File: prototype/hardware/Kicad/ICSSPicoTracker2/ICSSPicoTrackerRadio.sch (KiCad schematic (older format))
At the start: 85 parts, among them U11 74LVC1G04, U4 PE4259, U5 PE4259, U6 SX1276

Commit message: Updated Scehematics and Footprints
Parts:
- removed V01, V02, V03, V04, V05, V06: V-RF, symbol ICSSPicoTracker:V-RF
- added ANT?: Johanson434, symbol ICSSPicoTracker:Johanson434
- added ANT?: Johanson868, symbol ICSSPicoTracker:Johanson868
- added C75: 100nF, Capacitor_SMD:C_0603_1608Metric, symbol Device:C
- added X2: IQXO-70, Oscillator:Oscillator_SMD_SeikoEpson_SG210-4Pin_2.5x2.0mm, symbol Oscillator:IQXO-70
- C10, C11, C12, C14, C61, C8: value 100n -> 100nF; footprint (none) -> Capacitor_SMD:C_0603_1608Metric
- C13, C19, C31, C32, C42, C43, C50, C51, C57, C58, C59: value 47p -> 47pF; footprint (none) -> Capacitor_SMD:C_0402_1005Metric
- C15: value 10nf -> 10nF; footprint (none) -> Capacitor_SMD:C_0402_1005Metric
- C16, C17, C24: value 8p2 -> 8.2pF; footprint (none) -> Capacitor_SMD:C_0402_1005Metric
- C18: value 27p -> 27pF; footprint (none) -> Capacitor_SMD:C_0402_1005Metric
- C20: value 22p -> 22pF; footprint (none) -> Capacitor_SMD:C_0402_1005Metric
- C21: value 100p -> 100pF; footprint (none) -> Capacitor_SMD:C_0402_1005Metric
- C22, C26, C36, C37, C38, C40, C44, C45, C52, C53, C54, C55: footprint (none) -> Capacitor_SMD:C_0402_1005Metric
- C23: value 15p -> 15pF; footprint (none) -> Capacitor_SMD:C_0402_1005Metric
- C25, C35: value 56p -> 56pF; footprint (none) -> Capacitor_SMD:C_0402_1005Metric
- C27, C34: value 3p3 -> 3.3pF; footprint (none) -> Capacitor_SMD:C_0402_1005Metric
- C28: value 2p7 -> 2.7pF; footprint (none) -> Capacitor_SMD:C_0402_1005Metric
- C29: value 1p5 -> 1.5pF; footprint (none) -> Capacitor_SMD:C_0402_1005Metric
- C30, C39, C60: value 4p7 -> 4.7pF; footprint (none) -> Capacitor_SMD:C_0402_1005Metric
- C33: value 12p -> 12pF; footprint (none) -> Capacitor_SMD:C_0402_1005Metric
- C41: value 33p -> 33pF; footprint (none) -> Capacitor_SMD:C_0402_1005Metric
- C46, C47, C48, C49: value 1n -> 1nF; footprint (none) -> Capacitor_SMD:C_0402_1005Metric
- C56: value 220p -> 220pF; footprint (none) -> Capacitor_SMD:C_0402_1005Metric
- L10: value 10n -> 10nH; footprint (none) -> Inductor_SMD:L_0402_1005Metric
- L11: value 12n -> 12nH; footprint (none) -> Inductor_SMD:L_0402_1005Metric
- L12: value 4n7 -> 4.7nH; footprint (none) -> Inductor_SMD:L_0402_1005Metric
- L13, L16, L2, L8: value 47n -> 47nH; footprint (none) -> Inductor_SMD:L_0402_1005Metric
- L14, L5: value 18n -> 18nH; footprint (none) -> Inductor_SMD:L_0402_1005Metric
- L15, L17, L18, L19, L9: footprint (none) -> Inductor_SMD:L_0402_1005Metric
- L3: value 33n -> 33nH; footprint (none) -> Inductor_SMD:L_0402_1005Metric
- L4: value 100n -> 100nH; footprint (none) -> Inductor_SMD:L_0402_1005Metric
- L6: value 22n -> 22nH; footprint (none) -> Inductor_SMD:L_0402_1005Metric
- L7: value 5n6 -> 5.6nH; footprint (none) -> Inductor_SMD:L_0402_1005Metric
- R2, R3, R4, R5: footprint (none) -> Resistor_SMD:R_0603_1608Metric
- U11: footprint (none) -> Package_TO_SOT_SMD:SOT-353_SC-70-5
- U6: footprint (none) -> Package_DFN_QFN:QFN-28-1EP_6x6mm_P0.65mm_EP4.25x4.25mm_ThermalVias
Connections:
- net labels added: +1V8, RF_DIO0, RF_DIO1, RF_DIO2, RF_DIO3, RF_DIO4, RF_DIO5, RF_MISO, RF_MOSI, RF_NSEL, RF_RESET, RF_SCLK
- net labels removed: RF-CLK, RF-DIO0, RF-DIO5, RF-MISO, RF-MOSI, RF-NSEL, RF-RESET, RF-SCLK, RFSW-RX, RFSW-TX
- wire segments 257 -> 274
- no-connect marks 5 -> 3
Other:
- moved on the sheet: C14

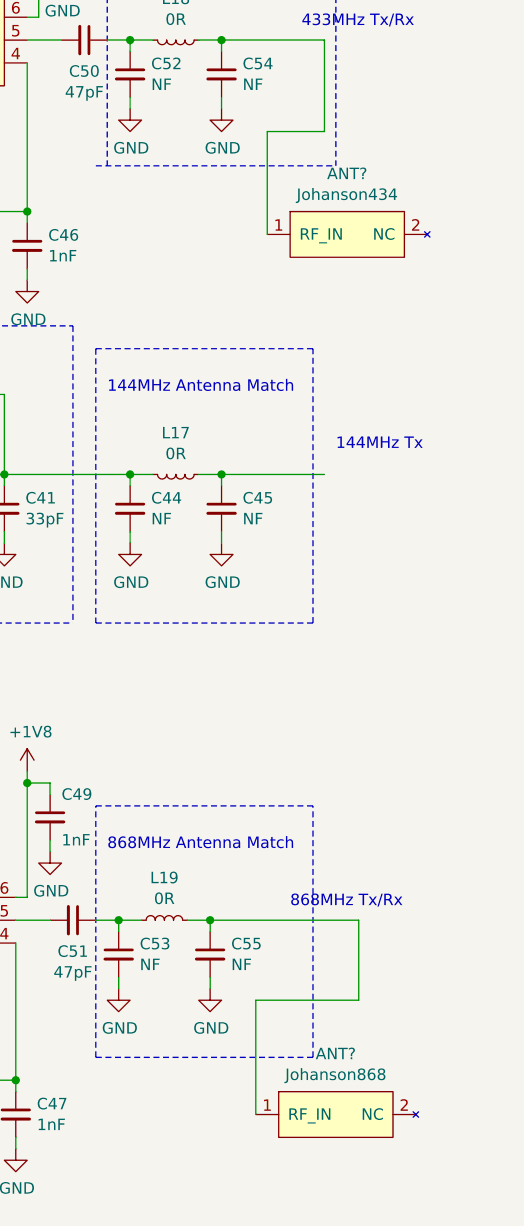
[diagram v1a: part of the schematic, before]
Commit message: Add Antenna footprints
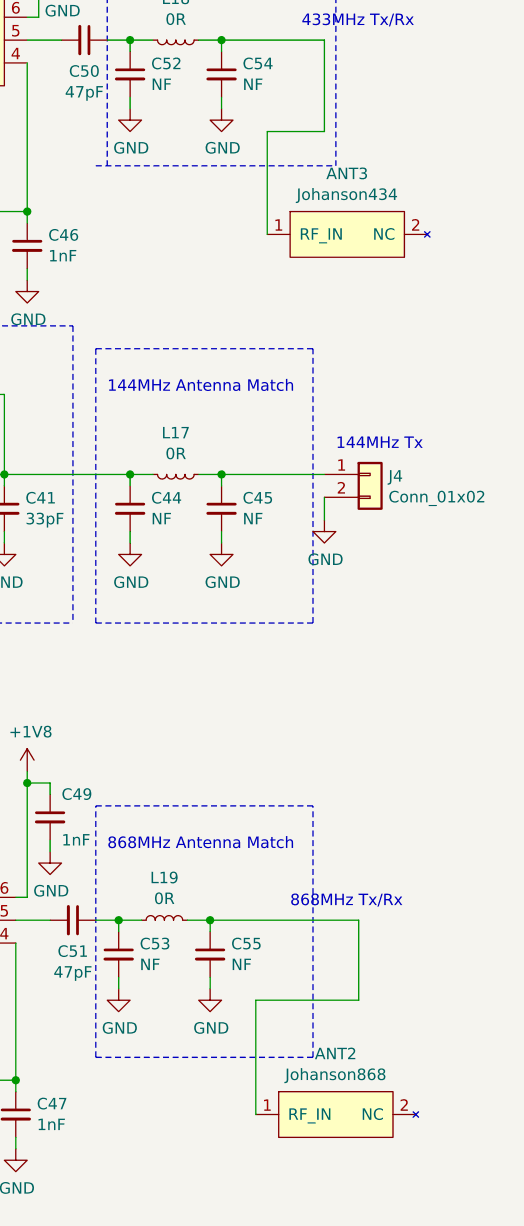
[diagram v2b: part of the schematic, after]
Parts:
- added J4: Conn_01x02, Connector_PinHeader_2.54mm:PinHeader_1x02_P2.54mm_Vertical, symbol Connector_Generic:Conn_01x02
- ANT2: renamed from ANT?; footprint (none) -> ICSSPicoTracker2:Johanson868
- ANT3: renamed from ANT?; footprint (none) -> ICSSPicoTracker2:Johanson434
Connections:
- net GND: now also J4.2 (Pin_2)
- net at C45.1, L17.1: now also J4.1 (Pin_1)
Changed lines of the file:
@@
 	1500 1750 1500 1800
 $Comp
-L ICSSPicoTracker:Johanson434 ANT?
+L ICSSPicoTracker:Johanson434 ANT3
 U 1 1 5D594580
 P 10850 2300
-F 0 "ANT?" H 10800 2565 50  0000 C CNN
+F 0 "ANT3" H 10800 2565 50  0000 C CNN
 F 1 "Johanson434" H 10800 2474 50  0000 C CNN
-F 2 "" H 10850 2300 50  0001 C CNN
+F 2 "ICSSPicoTracker2:Johanson434" H 10850 2300 50  0001 C CNN
 F 3 "" H 10850 2300 50  0001 C CNN
 	1    10850 2300
@@
 $EndComp
 $Comp
-L ICSSPicoTracker:Johanson868 ANT?
+L ICSSPicoTracker:Johanson868 ANT2
 U 1 1 5D59684D
 P 10800 6150
-F 0 "ANT?" H 10750 6415 50  0000 C CNN
+F 0 "ANT2" H 10750 6415 50  0000 C CNN
 F 1 "Johanson868" H 10750 6324 50  0000 C CNN
-F 2 "" H 10800 6150 50  0001 C CNN
+F 2 "ICSSPicoTracker2:Johanson868" H 10800 6150 50  0001 C CNN
 F 3 "" H 10800 6150 50  0001 C CNN
 	1    10800 6150
@@
 Wire Wire Line
 	10200 5300 10850 5300
+$Comp
+L Connector_Generic:Conn_01x02 J4
+U 1 1 5D5D0B50
+P 10900 3350
+F 0 "J4" H 10980 3342 50  0000 L CNN
+F 1 "Conn_01x02" H 10980 3251 50  0000 L CNN
+F 2 "Connector_PinHeader_2.54mm:PinHeader_1x02_P2.54mm_Vertical" H 10900 3350 50  0001 C CNN
+F 3 "~" H 10900 3350 50  0001 C CNN
+	1    10900 3350
+	1    0    0    -1
+$EndComp
+$Comp
+L power:GND #PWR0111
+U 1 1 5D5D1A65
+P 10700 3550
+F 0 "#PWR0111" H 10700 3300 50  0001 C CNN
+F 1 "GND" H 10705 3377 50  0000 C CNN
+F 2 "" H 10700 3550 50  0001 C CNN
+F 3 "" H 10700 3550 50  0001 C CNN
+	1    10700 3550
+	1    0    0    -1
+$EndComp
+Wire Wire Line
+	10700 3550 10700 3450
 $EndSCHEMATC

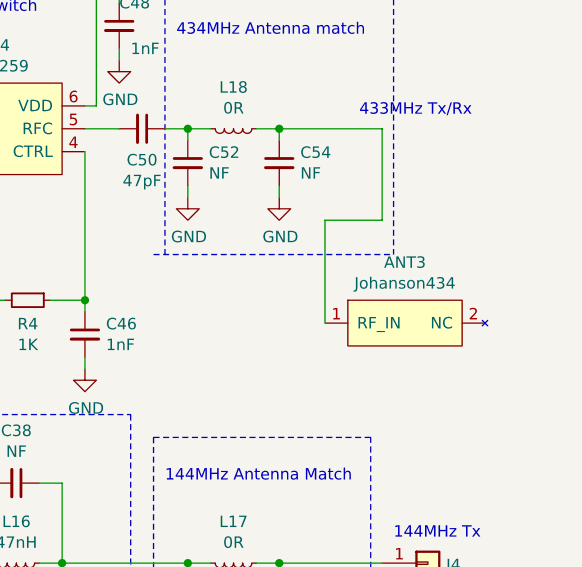
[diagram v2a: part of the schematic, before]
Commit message: Smaller Antenna and try some layouts
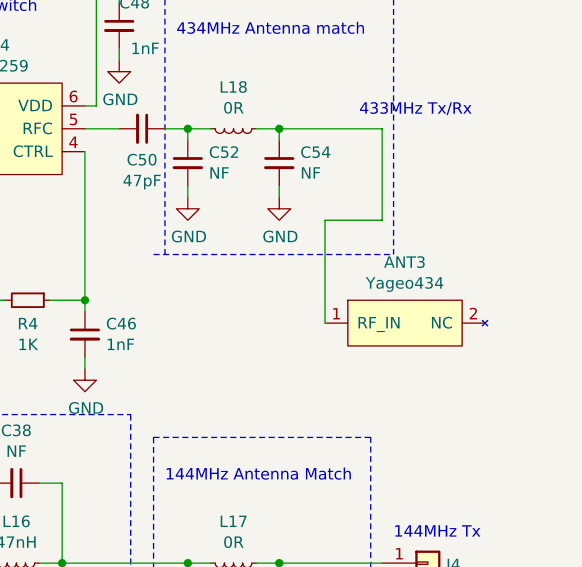
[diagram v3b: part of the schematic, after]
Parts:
- removed ANT3: Johanson434, ICSSPicoTracker2:Johanson434, symbol ICSSPicoTracker:Johanson434
- added ANT3: Yageo434, ICSSPicoTracker2:Yageo434, symbol ICSSPicoTracker:Yageo434
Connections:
- net at C54.1, L18.2: now also ANT3.1 (RF_IN)
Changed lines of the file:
@@
 	1500 1750 1500 1800
-$Comp
-L ICSSPicoTracker:Johanson434 ANT3
-U 1 1 5D594580
-P 10850 2300
-F 0 "ANT3" H 10800 2565 50  0000 C CNN
-F 1 "Johanson434" H 10800 2474 50  0000 C CNN
-F 2 "ICSSPicoTracker2:Johanson434" H 10850 2300 50  0001 C CNN
-F 3 "" H 10850 2300 50  0001 C CNN
-	1    10850 2300
-	1    0    0    -1
-$EndComp
 $Comp
 L ICSSPicoTracker:Johanson868 ANT2
@@
 Wire Wire Line
 	10700 3550 10700 3450
+$Comp
+L ICSSPicoTracker:Yageo434 ANT3
+U 1 1 5D656BA7
+P 10850 2300
+F 0 "ANT3" H 10800 2565 50  0000 C CNN
+F 1 "Yageo434" H 10800 2474 50  0000 C CNN
+F 2 "ICSSPicoTracker2:Yageo434" H 10850 2300 50  0001 C CNN
+F 3 "" H 10850 2300 50  0001 C CNN
+	1    10850 2300
+	1    0    0    -1
+$EndComp
 $EndSCHEMATC
